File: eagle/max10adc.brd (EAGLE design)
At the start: 98 x 62 mm, 209 parts, among them IC1 MAX19506, IC2 MAX19506, J1 MOLEX_BNC_73100-0105, J2 MOLEX_BNC_73100-0105, J3 MOLEX_BNC_73100-0105, J4 MOLEX_BNC_73100-0105, K1 AQY21SOP, K2 AQY21SOP, K3 AQY21SOP, K4 AQY21SOP, U1 MAX4416ESA, U2 MAX4416ESA, U340G CH340G, Y1 ABL-12.000MHZ-B2

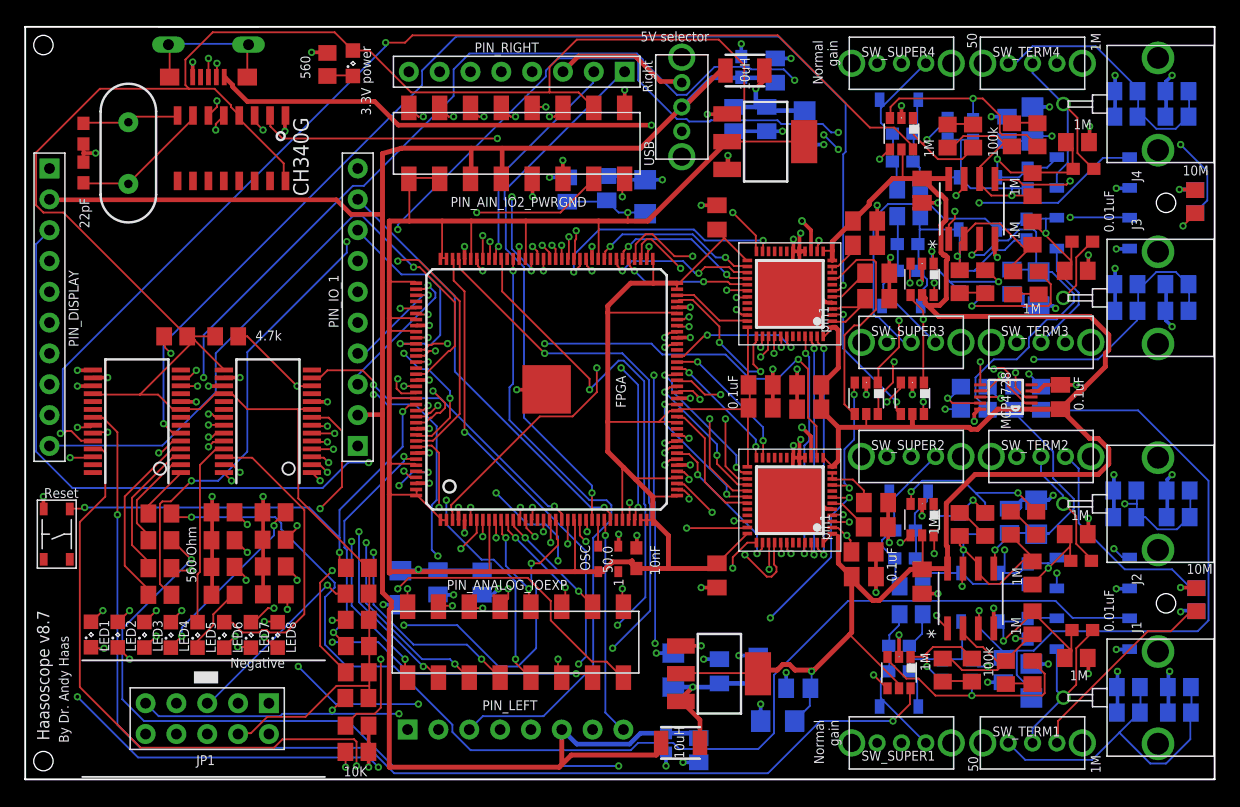
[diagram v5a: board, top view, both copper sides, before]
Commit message: v8.8 with 50pF low gain caps
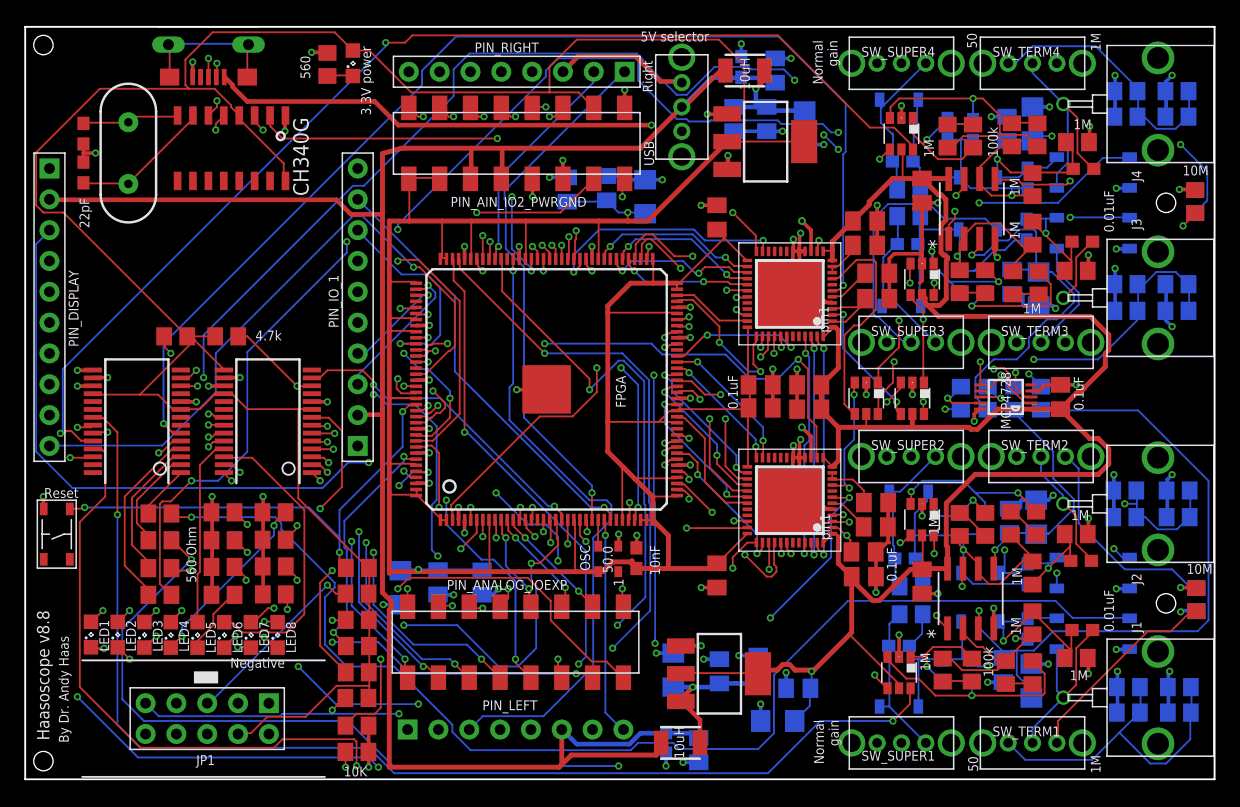
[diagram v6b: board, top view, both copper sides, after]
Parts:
- removed CIN56_1, CIN56_2, CIN56_3, CIN56_4: 56pF, rcl@1:C0603
- CGAIN1_1, CGAIN1_2, CGAIN1_3, CGAIN1_4: value 56pF -> 50pF
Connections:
- net INAMINUS1: no longer CIN56_1.2
- net INAMINUS2: no longer CIN56_3.2
- net INBMINUS1: no longer CIN56_2.2
- net INBMINUS2: no longer CIN56_4.2
- net N$20: no longer CIN56_1.1
- net N$38: no longer CIN56_2.1
- net N$40: no longer CIN56_3.1
- net N$42: no longer CIN56_4.1
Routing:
- net GND: track 222.5 -> 231.6 mm, vias 102 -> 99
- net N$38: track 15.0 -> 13.2 mm
- net INAMINUS2: track 35.8 -> 36.9 mm
- net N$20: track 13.7 -> 13.1 mm
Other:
- board text added: "Haasoscope v8.8"
- board text removed: "Haasoscope v8.7"
